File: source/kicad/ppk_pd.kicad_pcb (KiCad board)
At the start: 2 copper layers, 4 parts

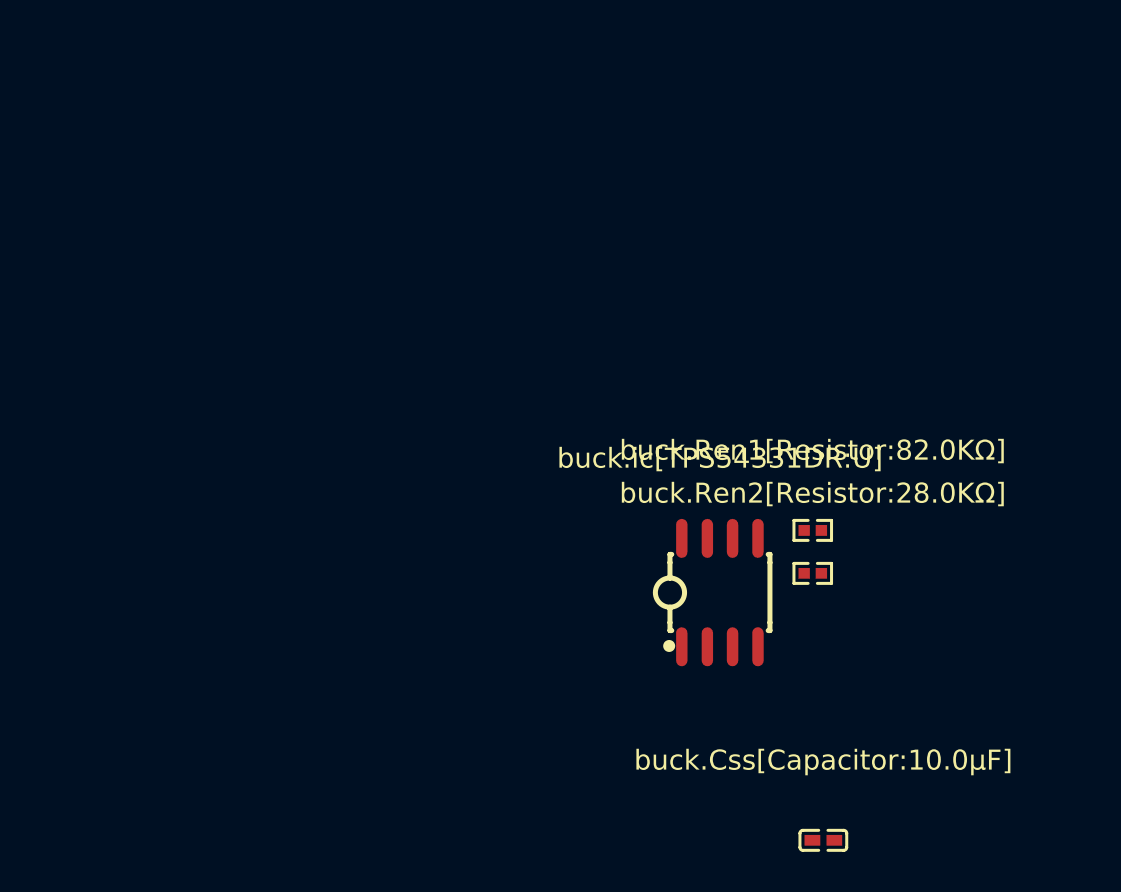
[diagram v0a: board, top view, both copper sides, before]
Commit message: Better logging, add header and try adding designators
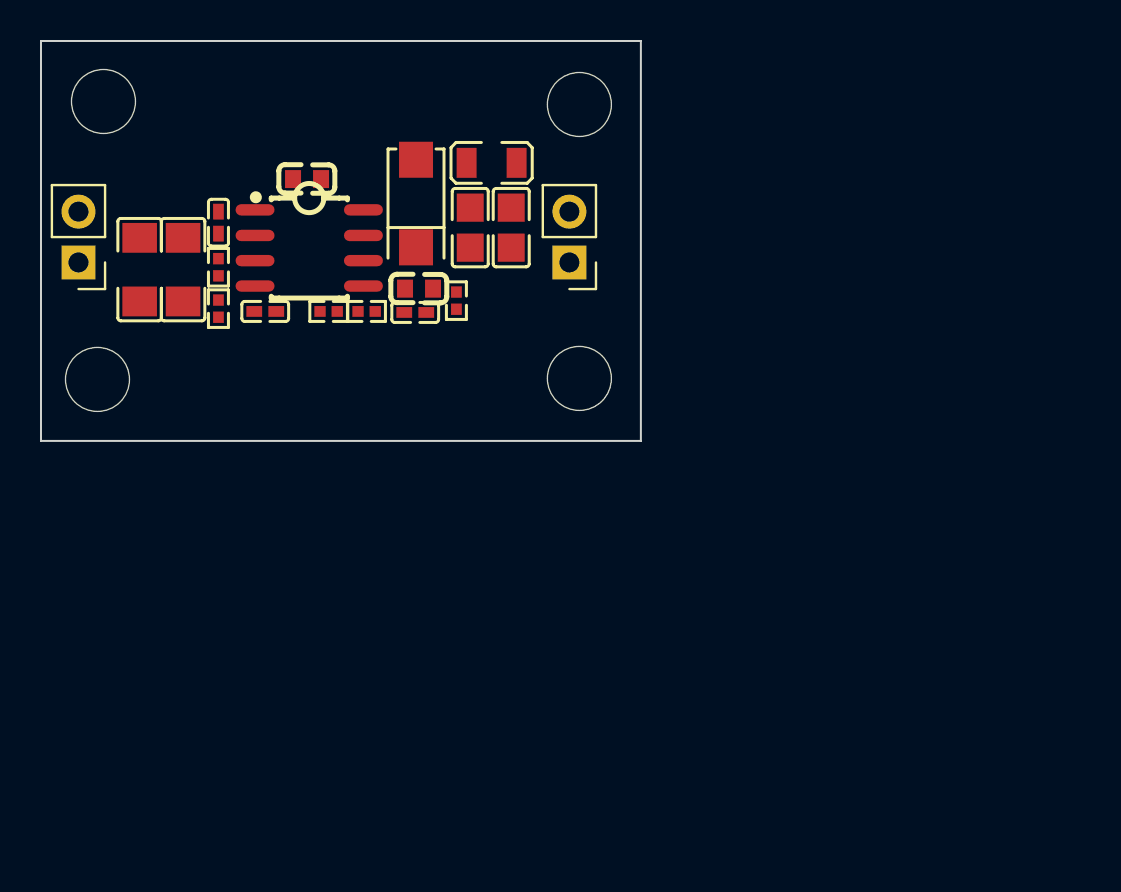
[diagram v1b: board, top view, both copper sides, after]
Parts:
- removed buck.Css[Capacitor:10.0µF]: 10.0µF, lcsc:C0402
- removed buck.Ren1[Resistor:82.0KΩ]: 82.0KΩ, lcsc:R0402
- removed buck.Ren2[Resistor:28.0KΩ]: 28.0KΩ, lcsc:R0402
- removed buck.ic[TPS54331DR:U]: U, lcsc:SOIC-8_L5.0-W4.0-P1.27-LS6.0-BL
- added buck.C1[Capacitor:2.2uF]: 2.2uF, lcsc:C1206, F.Cu at (51.9, 39.4)
- added buck.C2[Capacitor:2.2uF]: 2.2uF, lcsc:C1206, F.Cu at (54.1, 39.4)
- added buck.C3[Capacitor:10nF]: 10nF, lcsc:C0402, F.Cu at (55.9, 37.1)
- added buck.C4[Capacitor:100nF]: 100nF, lcsc:C0603, F.Cu at (60.3, 34.9)
- added buck.C5[Capacitor:10nF]: 10nF, lcsc:C0402, F.Cu at (58.2, 41.5)
- added buck.C6[Capacitor:4.7nF]: 4.7nF, lcsc:C0402, F.Cu at (65.7, 41.6)
- added buck.C7[Capacitor:200pF]: 200pF, lcsc:C0603, F.Cu at (65.9, 40.4)
- added buck.C8[Capacitor:22uF]: 22uF, lcsc:C0805, F.Cu at (68.5, 37.3)
- added buck.C9[Capacitor:22uF]: 22uF, lcsc:C0805, F.Cu at (70.5, 37.3)
- added buck.D1[Diode:D]: D, lcsc:SMA_L4.4-W2.6-LS5.0-RD, F.Cu at (65.8, 36.1)
- added buck.L1[Inductor:47uH]: 47uH, lcsc:IND-SMD_L2.5-W2.0-A, F.Cu at (69.5, 34.1)
- added buck.R1[Resistor:82k]: 82k, lcsc:R0402, F.Cu at (55.9, 39.3)
- added buck.R2[Resistor:29.4k]: 29.4k, lcsc:R0402, F.Cu at (55.9, 41.4)
- added buck.R3[Resistor:6.8k]: 6.8k, lcsc:R0402, F.Cu at (67.8, 41.0)
- added buck.R5[Resistor:10k]: 10k, lcsc:R0402, F.Cu at (63.3, 41.5)
- added buck.R6[Resistor:2.49k]: 2.49k, lcsc:R0402, F.Cu at (61.4, 41.5)
- added buck.U1[TPS54331DR:U]: U, lcsc:SOIC-8_L5.0-W4.0-P1.27-LS6.0-BL, F.Cu at (60.4, 38.4)
- added input_header[Pin_Header:J]: J, Connector_PinHeader_2.54mm:PinHeader_1x02_P2.54mm_Vertical, F.Cu at (48.9, 39.1)
- added mounting_hole[0][Mounting_Hole:H]: H, MountingHole:MountingHole_3.2mm_M3_ISO7380, F.Cu at (50.1, 31.0)
- added mounting_hole[1][Mounting_Hole:H]: H, MountingHole:MountingHole_3.2mm_M3_ISO7380, F.Cu at (73.9, 31.2)
- added mounting_hole[2][Mounting_Hole:H]: H, MountingHole:MountingHole_3.2mm_M3_ISO7380, F.Cu at (49.8, 44.9)
- added mounting_hole[3][Mounting_Hole:H]: H, MountingHole:MountingHole_3.2mm_M3_ISO7380, F.Cu at (73.9, 44.9)
- added output_header[Pin_Header:J]: J, Connector_PinHeader_2.54mm:PinHeader_1x02_P2.54mm_Vertical, F.Cu at (73.4, 39.1)
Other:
- board outline added: 30 x 20 mm
